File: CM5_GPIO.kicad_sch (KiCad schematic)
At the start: 26 parts, among them J14 JST_SHBM04B-SRSS-TB, J2 Conn_02x07_Odd_Even, J3 Conn_01x03, J7 Micro_SD_Card_Det, J8 THD-20-R, J9 THD-02-R, SW1 Right angle Tact button, U1 TPD4EUSB30, U18 RT9742GGJ5, U2 TPD4EUSB30, U3 MagJack-A70-112-331N126, U5 74LVC1G07SE-7

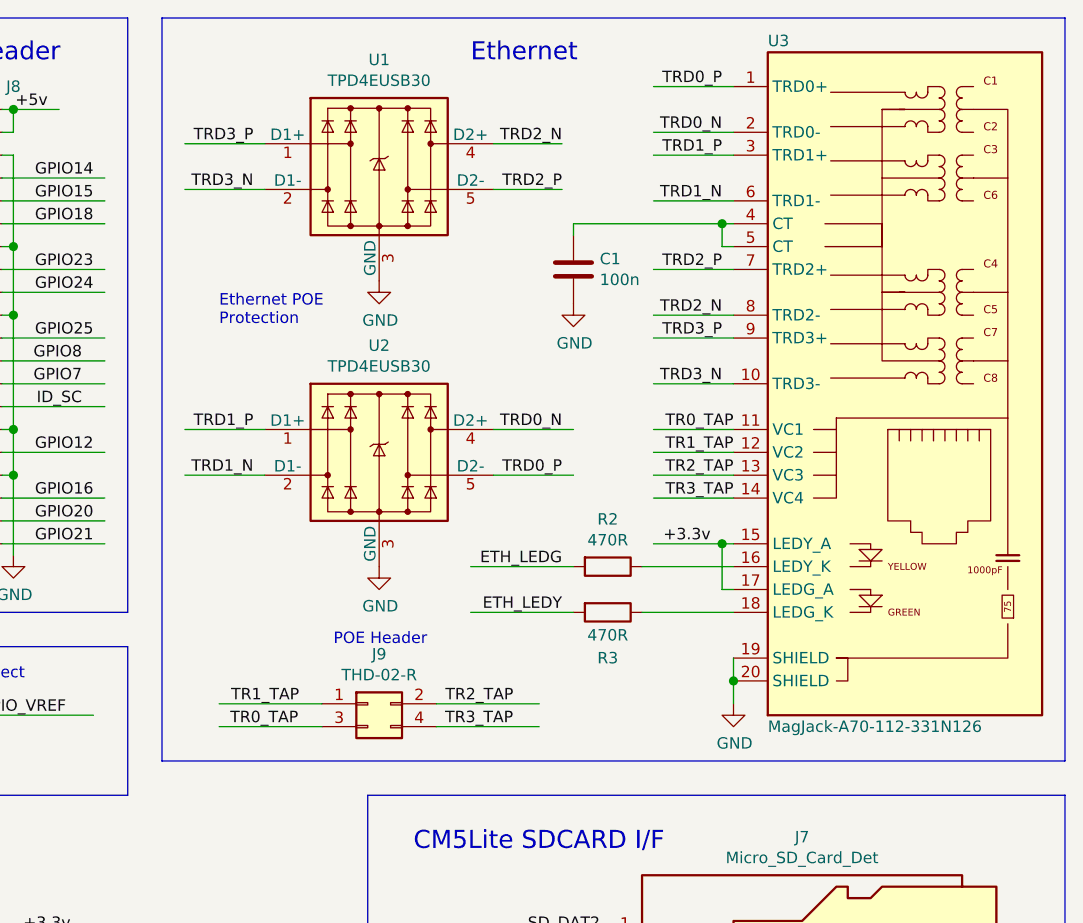
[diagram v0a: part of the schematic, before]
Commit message: remove ethernet, pcie, hdmi
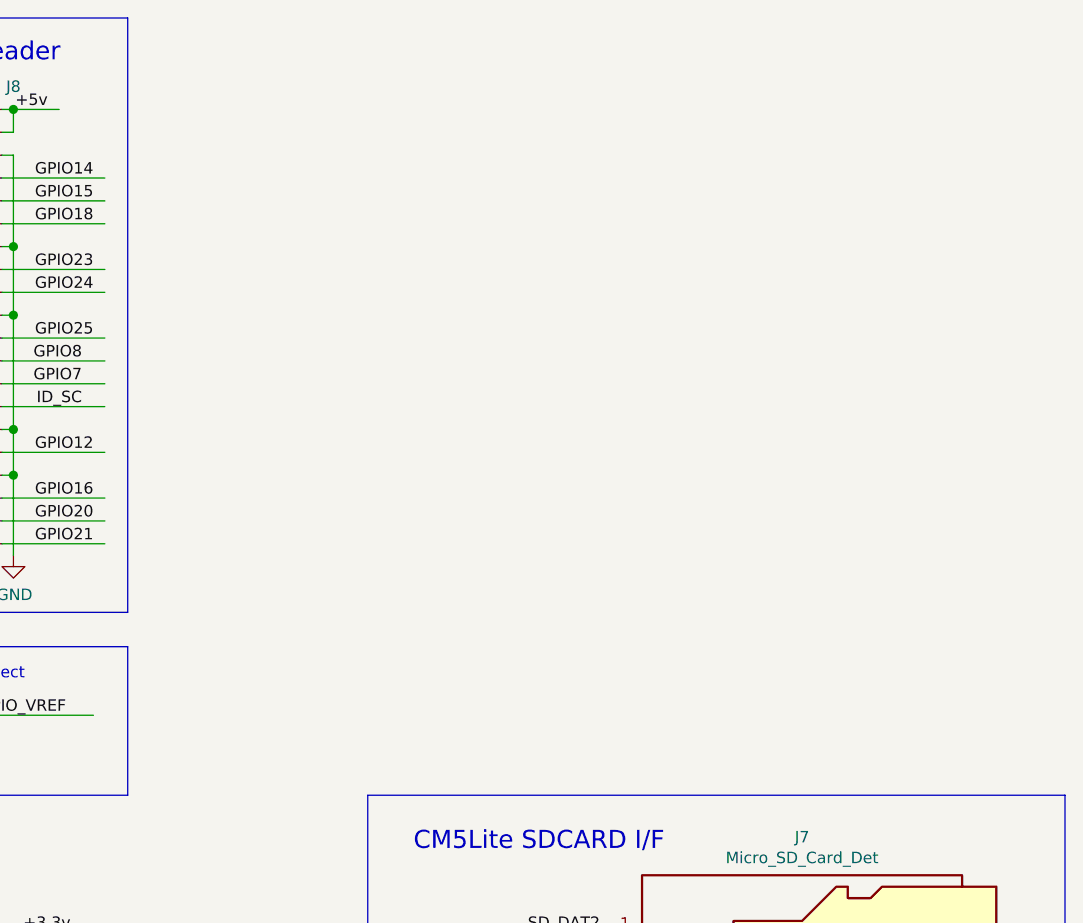
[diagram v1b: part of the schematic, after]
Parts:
- removed C1: 100n, Capacitor_SMD:C_0402_1005Metric, symbol Device:C
- removed J9: THD-02-R, Connector_PinHeader_2.54mm:PinHeader_2x02_P2.54mm_Vertical, symbol Connector_Generic:Conn_02x02_Odd_Even
- removed R2, R3: 470R, Resistor_SMD:R_0402_1005Metric, symbol Device:R
- removed U1, U2: TPD4EUSB30, Package_SON:USON-10_2.5x1.0mm_P0.5mm, symbol CM5IO:TPD4EUSB30
- removed U3: MagJack-A70-112-331N126, CM5IO:TRJG0926HENL, symbol CM5IO:MagJack-A70-112-331N126
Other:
- note removed: "Ethernet"
- note removed: "Ethernet POE Protection"
- note removed: "POE Header"
